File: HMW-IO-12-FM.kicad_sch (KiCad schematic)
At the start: 64 parts, among them IC1 ATmega32A-A, IC2 ATmega32A-M, IC3 MAX487E, IC4 MC34063AD, J1 Conn_01x04_Male, J2 Conn_01x04_Male, J3 Screw_Terminal_01x06, J4 BUS_Terminal, Q1 16Mhz

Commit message: Add files via upload
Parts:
- D3: footprint Diode_SMD:D_SMA_Handsoldering -> Diode_SMD:D_MELF
- L1: footprint Inductor_SMD:L_Bourns_SRN6045TA -> Inductor_SMD:L_Taiyo-Yuden_MD-4040
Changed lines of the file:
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@@
       (effects (font (size 1.27 1.27)) (justify left))
     )
-    (property "Footprint" "Diode_SMD:D_SMA_Handsoldering" (id 2) (at 136.017 170.688 0)
+    (property "Footprint" "Diode_SMD:D_MELF" (id 2) (at 136.017 170.688 0)
       (effects (font (size 1.27 1.27)) hide)
     )
@@
       (effects (font (size 1.27 1.27)) (justify right))
     )
-    (property "Footprint" "Inductor_SMD:L_Bourns_SRN6045TA" (id 2) (at 133.858 170.688 0)
+    (property "Footprint" "Inductor_SMD:L_Taiyo-Yuden_MD-4040" (id 2) (at 133.858 170.688 0)
       (effects (font (size 1.27 1.27)) hide)
     )
@@
     )
     (path "/a83c71b2-c557-4318-8baf-b665aa48616f"
-      (reference "D3") (unit 1) (value "SK14") (footprint "Diode_SMD:D_SMA_Handsoldering")
+      (reference "D3") (unit 1) (value "SK14") (footprint "Diode_SMD:D_MELF")
     )
     (path "/7eeefaeb-2380-44de-a045-b8d6373a8872"
@@
     )
     (path "/bc0bae93-6b92-4c09-b2b0-40b90b780a49"
-      (reference "L1") (unit 1) (value "270µH") (footprint "Inductor_SMD:L_Bourns_SRN6045TA")
+      (reference "L1") (unit 1) (value "270µH") (footprint "Inductor_SMD:L_Taiyo-Yuden_MD-4040")
     )
     (path "/2664d110-8418-4b55-9263-cbd1700b6a20"

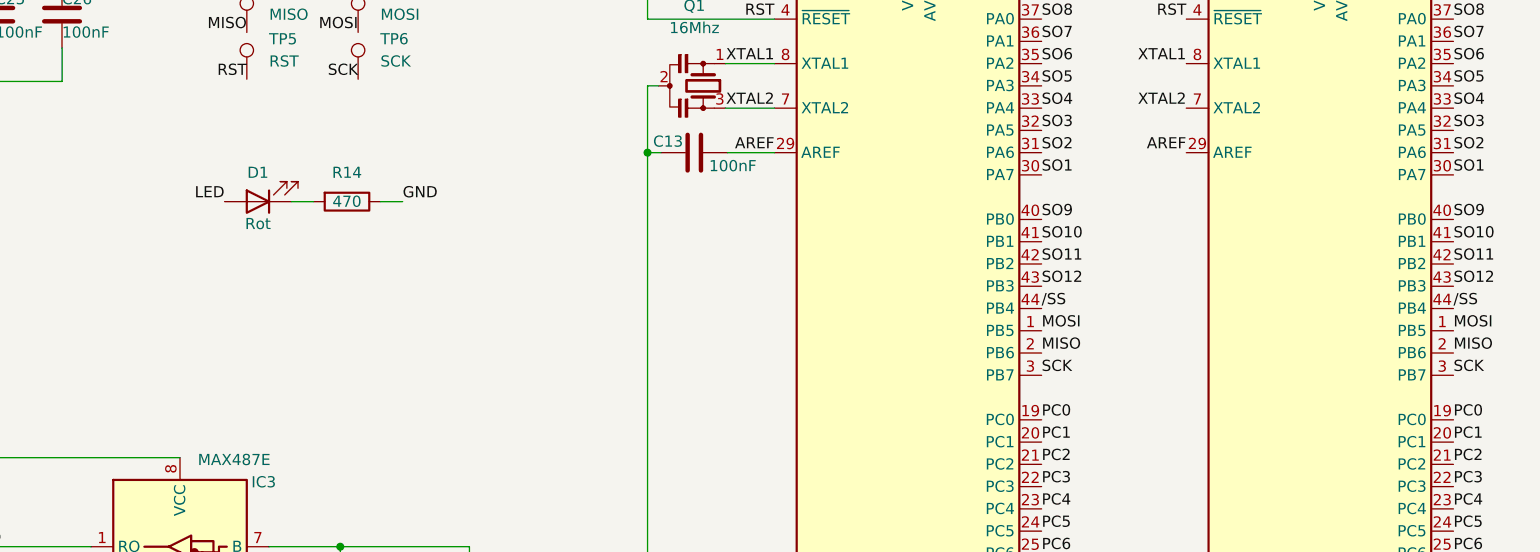
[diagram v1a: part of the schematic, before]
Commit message: Add button for firmware reset.
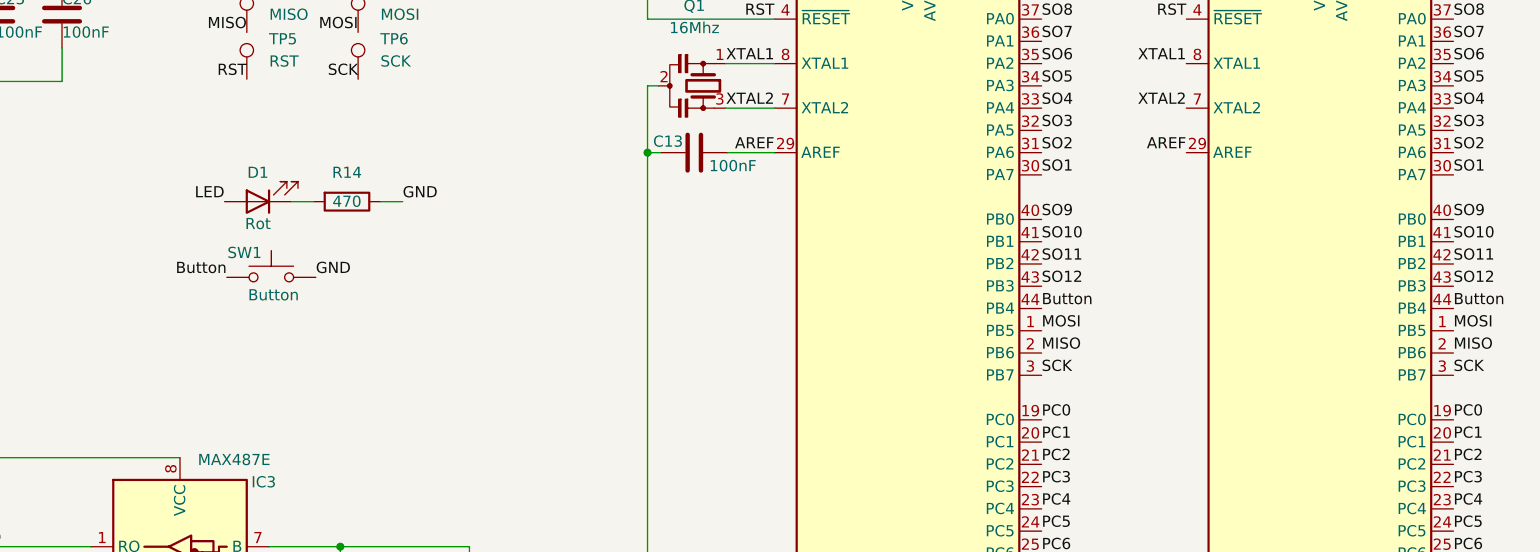
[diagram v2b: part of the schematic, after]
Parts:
- added SW1: Button, Button_Switch_SMD:SW_Push_1P1T_NO_CK_KMR2, symbol Switch:SW_Push
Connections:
- net GND: now also SW1.2
- net /SS renamed Button
- net Button: now also SW1.1
